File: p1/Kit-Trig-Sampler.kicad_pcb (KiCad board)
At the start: 2 copper layers, 78 x 109.2 mm, 85 parts, among them J1 START_CV, J10 AUDIO_INR, J11 AUDIO_OUTL, J13 BANK_CV, J14 Eurorack_Power_16pin_Unshroud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, J2 LENGTH_CV, J3 SAMP_CV, J4 PITCH CV, J5 REV_TRIG, J6 PLAY_TRIG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

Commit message: changes to schem and layout
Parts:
- added R35: 33k_TH0.125, 4ms_Resistor:R_Axial_DIN0207_L6.3mm_D2.5mm_P7.62mm_Horizontal, F.Cu at (27.0, 72.7)
- added R37: 10k_TH0.125, 4ms_Resistor:R_Axial_DIN0207_L6.3mm_D2.5mm_P7.62mm_Horizontal, F.Cu at (87.8, 64.8)
- C19: value 10uF_Radial_TH -> 47uF_16V_TH
- R25, R26, R27: value 4.7k_TH0.125 -> 10k_TH0.125
- R9: value 620Ω_TH0.125 -> 10k_TH0.125
- U3: footprint Package_TO_SOT_THT:TO-220-3_Vertical -> 4ms_Package_TO:TO-220-3_PXO7803
- moved R14 6.29 mm to (15.1, 79.5), turned to -90 degrees
- moved R9 5.97 mm to (87.8, 74.9)
- moved C19 5.65 mm to (69.1, 24.2)
- moved C15 5.64 mm to (21.4, 69.5), turned to 0 degrees
- moved R1 5.59 mm to (87.7, 84.8)
- moved U3 4.39 mm to (64.3, 21.2), turned to 90 degrees
- moved R31 3.99 mm to (56.5, 52.2)
- moved C11 2.56 mm to (16.4, 72.9)
- moved R15 1.58 mm to (14.2, 89.4)
- moved R33 1.23 mm to (52.2, 94.5)
- moved R13 0.18 mm to (27.0, 75.6)
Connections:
- C3 pad 2: Net-(C3-Pad2) -> Net-(U1B-+)
- R11 pad 1: Net-(C3-Pad2) -> Net-(U1B-+)
- R13 pad 1: GND -> Net-(R13-Pad1)
- R9 pad 2: Net-(C3-Pad2) -> Net-(R37-Pad1)
- U1 pad 5: Net-(C3-Pad2) -> Net-(U1B-+)
- U2 pad 5: (no net) -> GND
- U2 pad 6: (no net) -> Net-(U2B--)
- U2 pad 7: (no net) -> Net-(U2B--)
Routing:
- net Net-(C3-Pad2): track 14.4 -> 0.00 mm
- net Net-(U1B-+): track 0.00 -> 12.6 mm
- net -12VA: track 203.8 -> 213.4 mm, vias 6 -> 7
- net GND: track 515.4 -> 522.3 mm
- net Net-(U2A--): track 11.1 -> 17.6 mm
- net Net-(U1A-+): track 17.2 -> 22.7 mm
- net Net-(C11-Pad2): track 19.4 -> 23.3 mm
- net /D16: track 23.4 -> 19.8 mm
- net Net-(R13-Pad1): track 0.00 -> 2.90 mm
- net Net-(U2B--): track 0.00 -> 2.54 mm
- net Net-(R37-Pad1): track 0.00 -> 2.40 mm
- net +12V: track 233.9 -> 235.4 mm
- net Net-(J13-SIG): track 13.6 -> 12.4 mm
- net /A4: track 21.8 -> 20.6 mm
- net Net-(J4-SIG): track 15.9 -> 17.0 mm
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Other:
- board text added: "SAMPLER KIT p1"
- board text removed: "STS KIT p1"

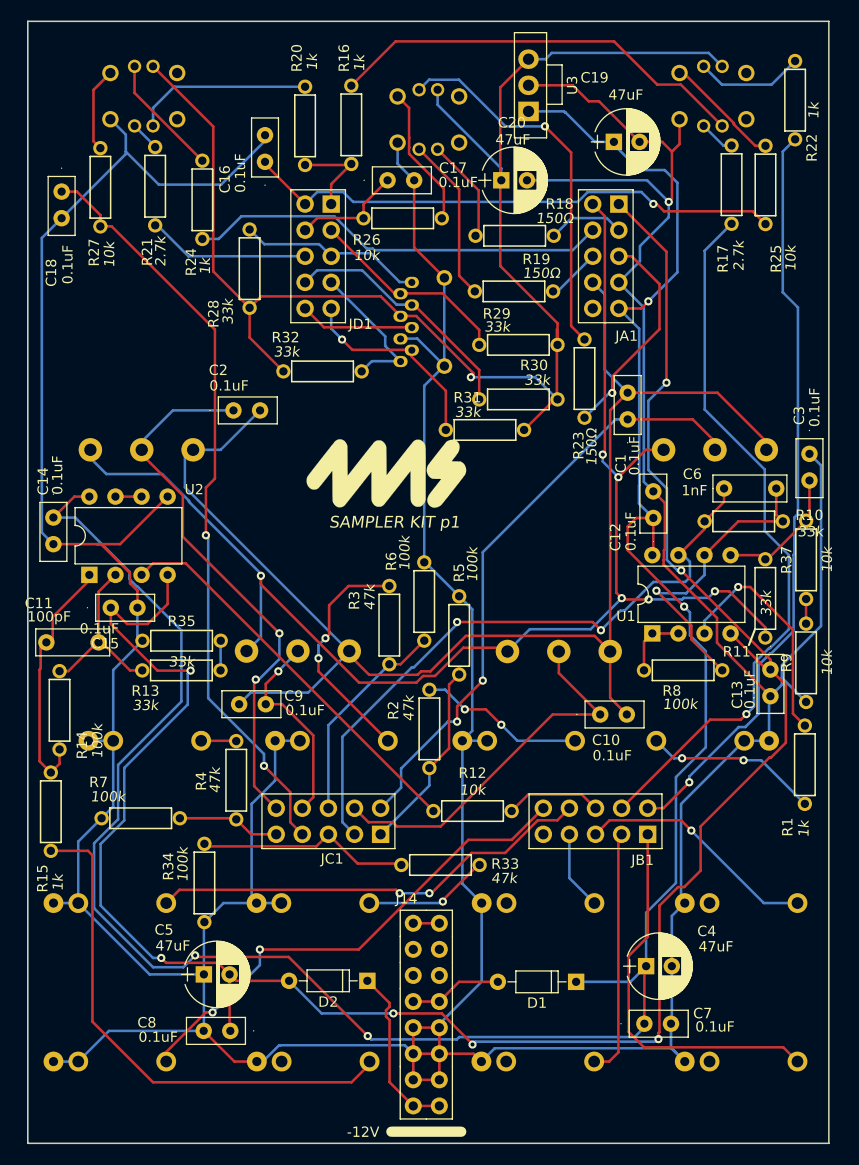
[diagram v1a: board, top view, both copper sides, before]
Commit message: updates to PCB. arrangement of silk.
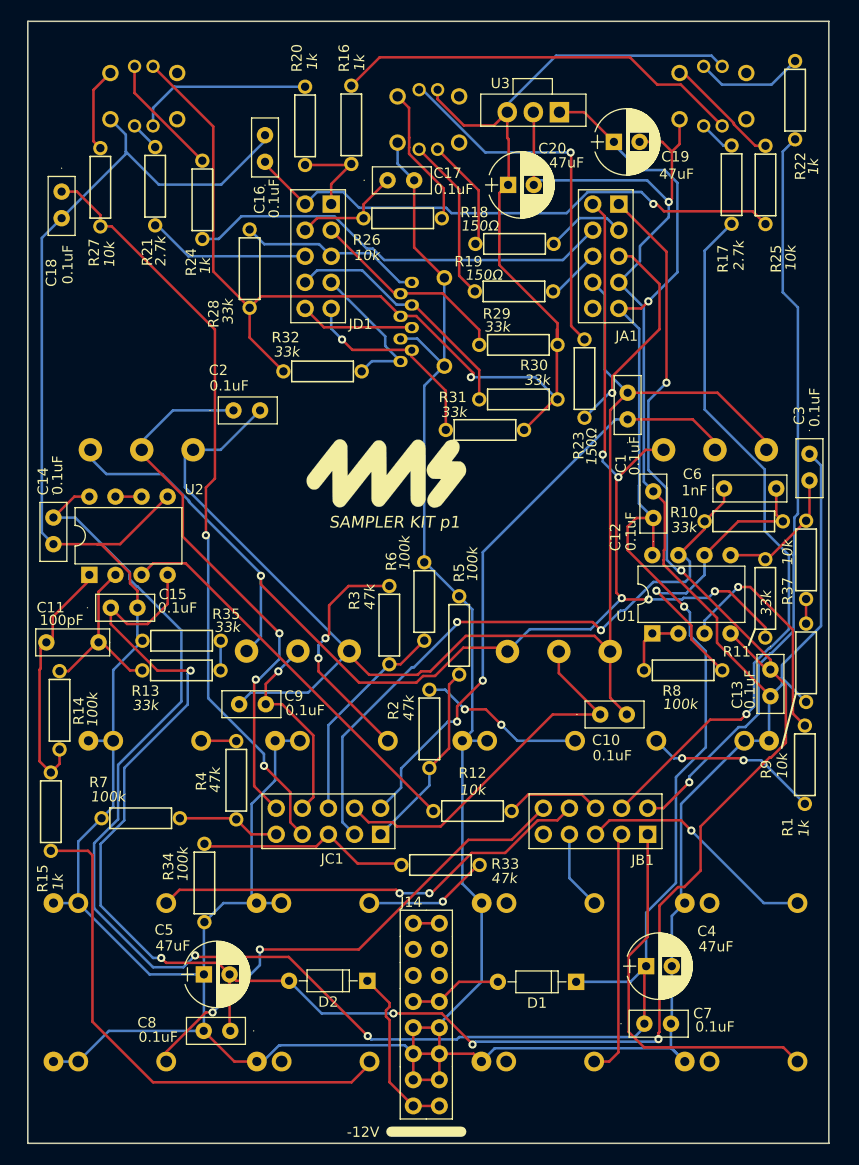
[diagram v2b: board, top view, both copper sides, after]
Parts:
- moved U3 3.48 mm to (63.8, 17.8), turned to 180 degrees
- moved C20 0.80 mm to (58.8, 28.4)
- moved R18 0.79 mm to (59.4, 34.1)
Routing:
- net GND: track 522.3 -> 515.3 mm
- net +3V3: track 143.7 -> 140.2 mm
- net +12V: track 235.4 -> 232.6 mm
- net Net-(Bank_But1-B): track 41.3 -> 40.0 mm
- net Net-(PLAY_BUT1-B): track 9.77 -> 11.0 mm
- net /D6: track 52.9 -> 53.8 mm
- net Net-(PLAY_BUT1-G): track 36.9 -> 36.1 mm
- net /D10: track 41.1 -> 41.9 mm

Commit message: Resistor Consolidation
and updates to Button LEDS
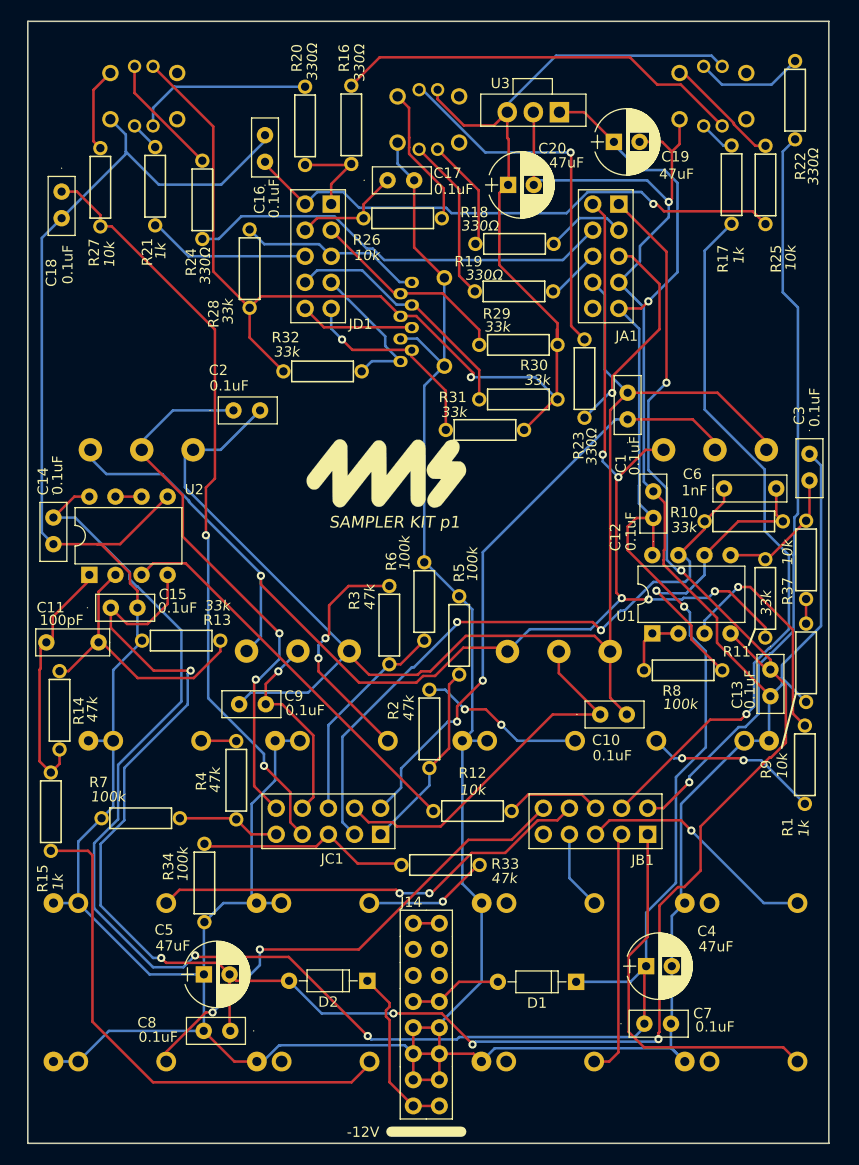
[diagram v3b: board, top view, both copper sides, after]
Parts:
- removed R35: 33k_TH0.125, 4ms_Resistor:R_Axial_DIN0207_L6.3mm_D2.5mm_P7.62mm_Horizontal
- R13: value 68k_TH0.125 -> 33k_TH0.125
- R14: value 100k_TH0.125 -> 47k_TH0.125
- R16, R20, R22, R24: value 1k_TH0.125 -> 330Ω_TH0.125
- R17, R21: value 2.7k_TH0.125 -> 1k_TH0.125
- R18, R19, R23: value 150Ω_TH0.125 -> 330Ω_TH0.125
- moved R13 2.90 mm to (26.9, 72.7), turned to 0 degrees
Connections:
- R13 pad 1: Net-(R13-Pad1) -> GND
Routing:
- net Net-(U2A--): track 17.6 -> 27.6 mm
- net Net-(R13-Pad1): track 2.90 -> 0.00 mm
